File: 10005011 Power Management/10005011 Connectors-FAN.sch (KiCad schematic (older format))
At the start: 63 parts, among them IC25 L78M24CDT, IC6 TLV3012AIDBV, J10 BATTERY, J6 FAN, J7 CPU BOARD, J9 TURBINE, T23 IRLML2803, T31 IRLML5103

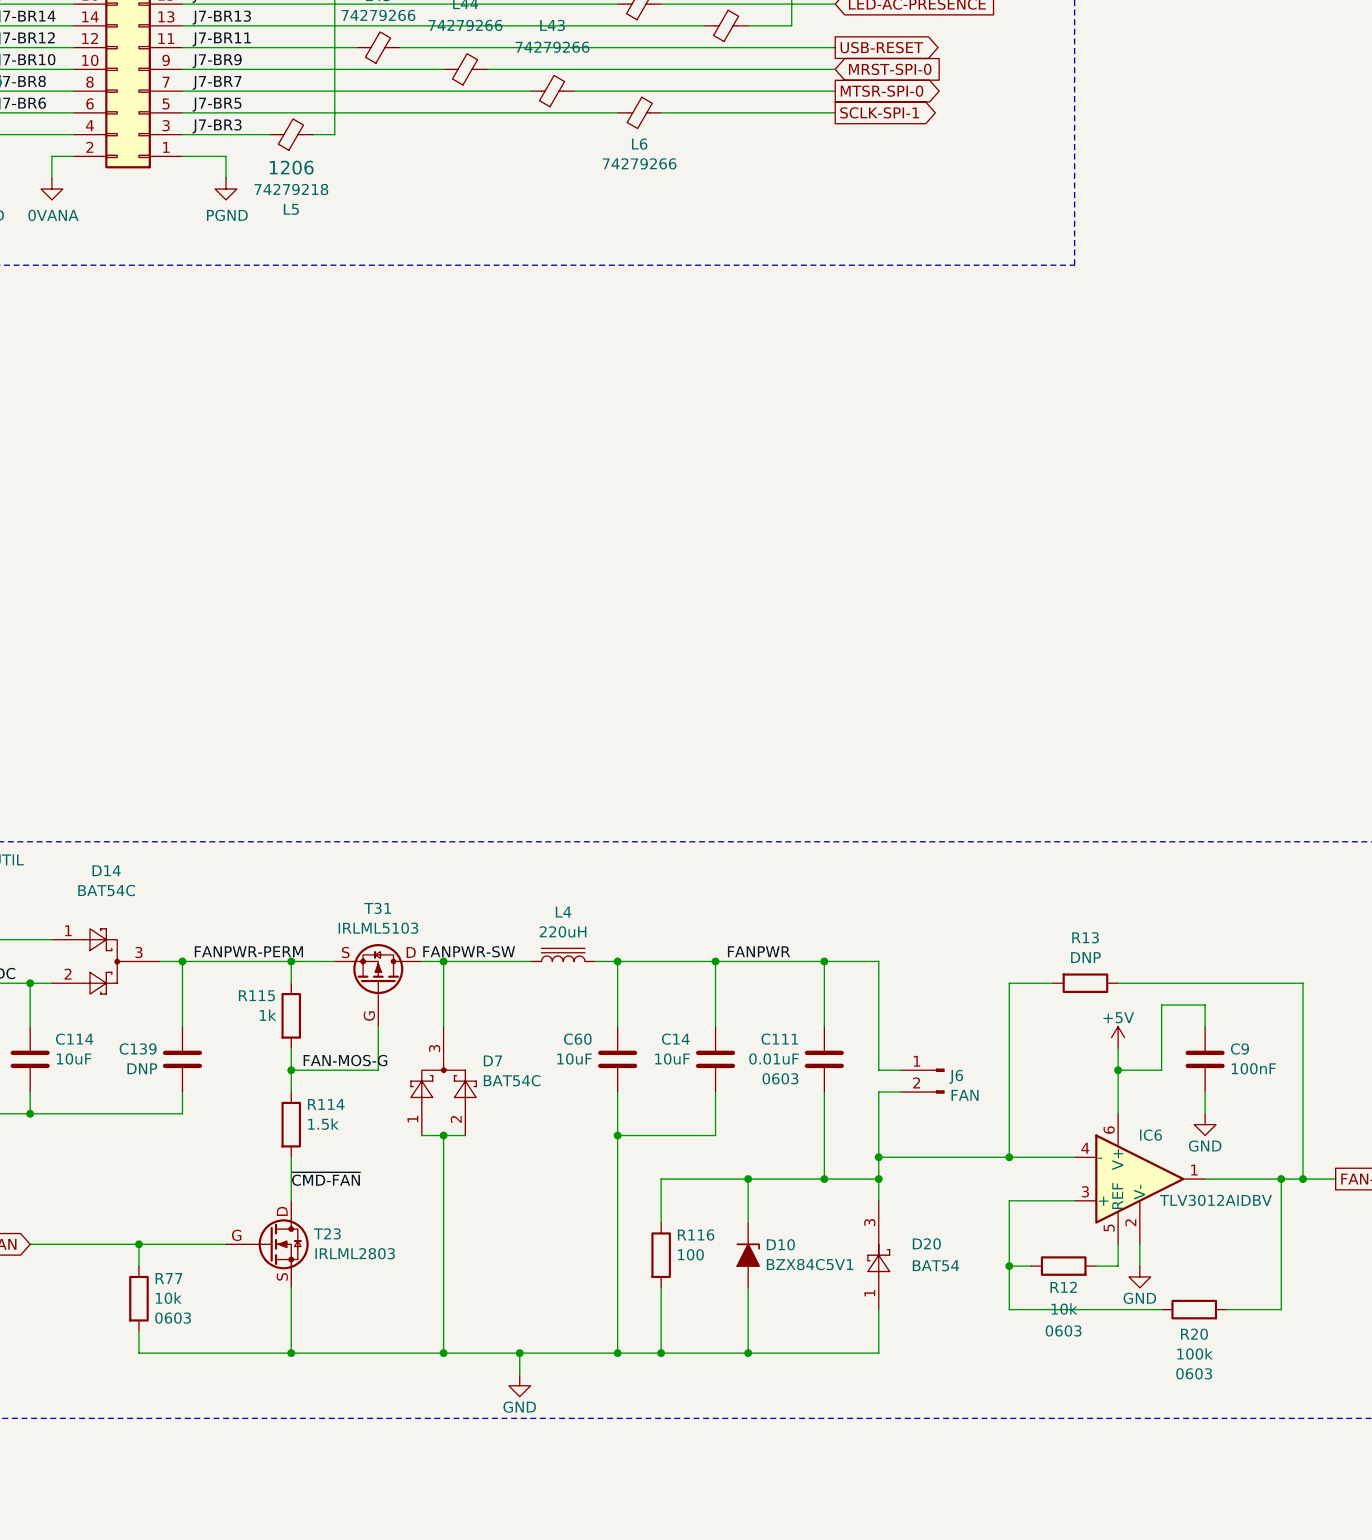
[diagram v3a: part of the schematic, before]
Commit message: Power managmt: fields updated from library, and non-library fields removed
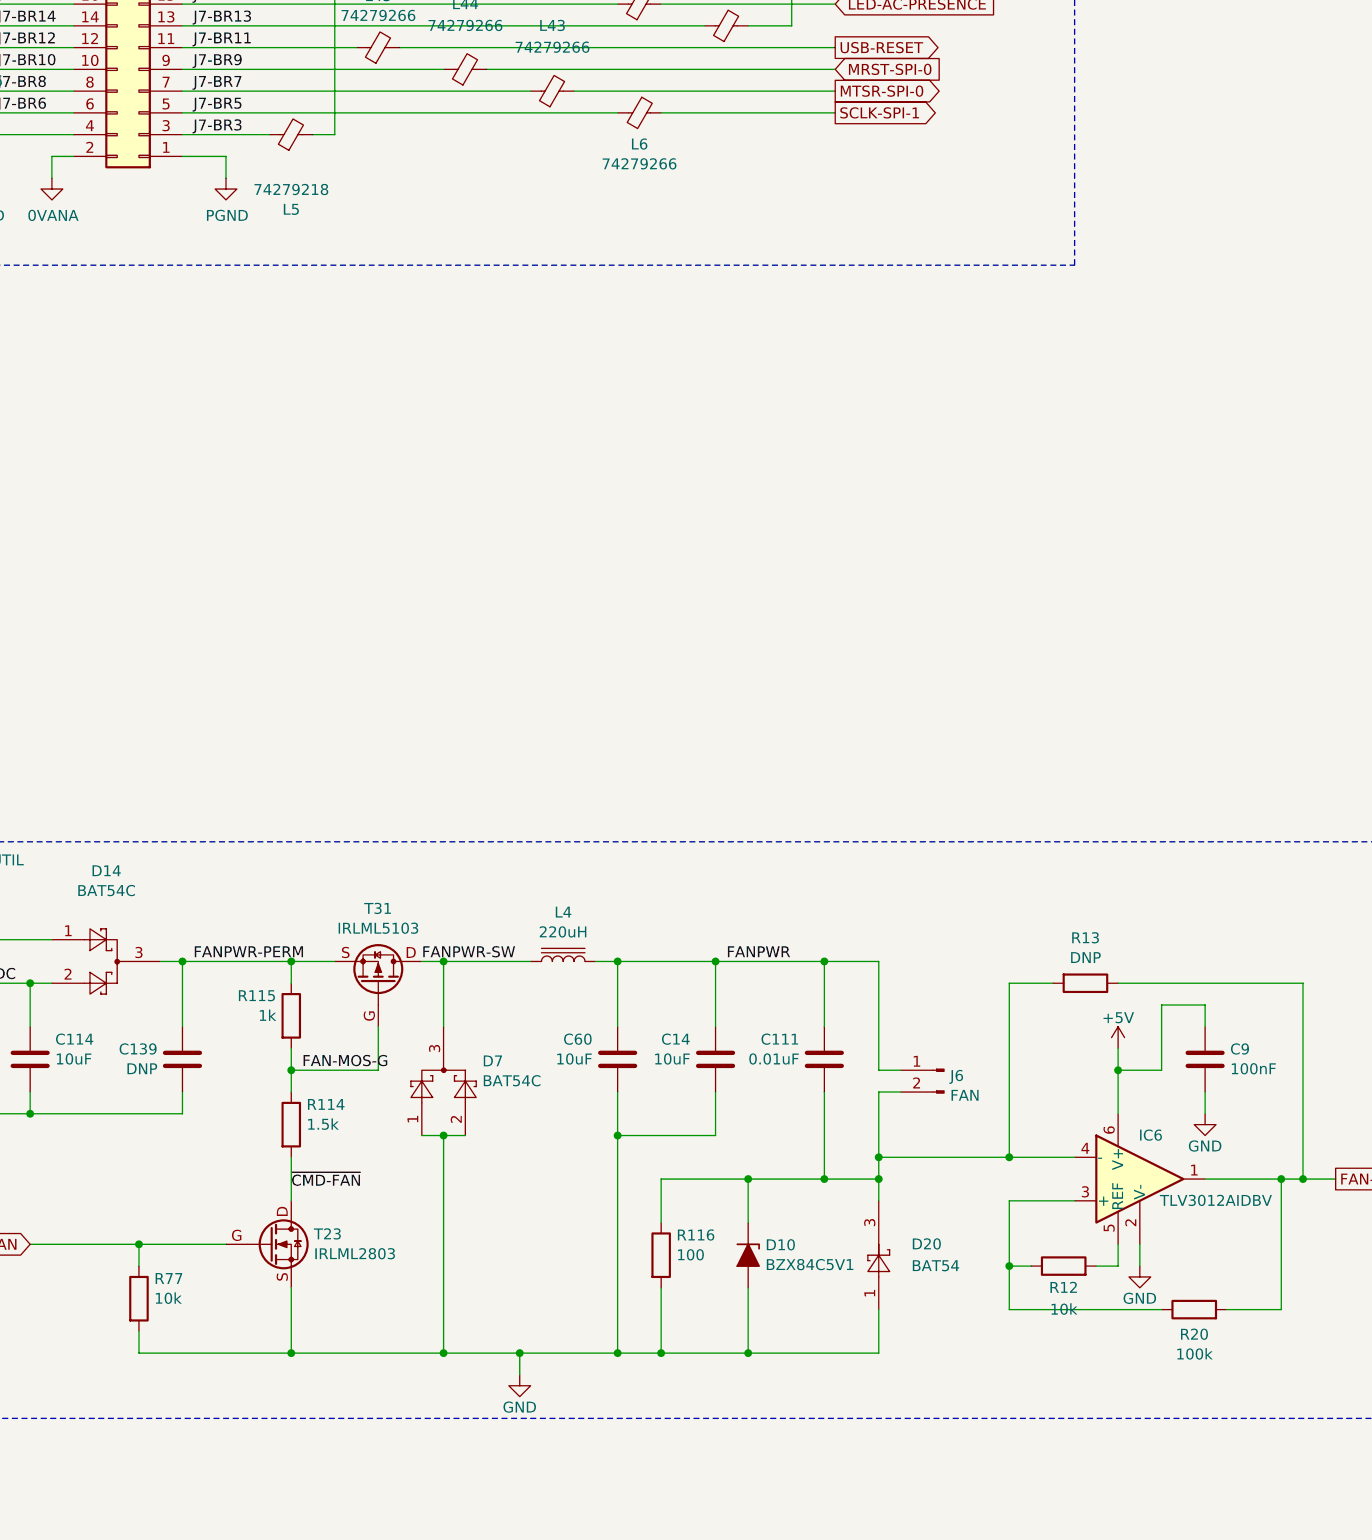
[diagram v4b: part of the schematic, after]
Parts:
- C10, C114, C14, C60: Description CAPACITOR CERAMIC, 10UF,+/-10%,50V -> CAPACITOR CERAMIC, 10UF,+/-10%,50V 2220; Dielectric X7R -> (none); Manufacturer2 (none) -> KEMET_RMS1; Manufacturer3 (none) -> KEMET_RMS1; Manufacturer_No2 (none) -> C2220X106K5RACAUTO; Manufacturer_No3 (none) -> C2220X106K5RAC; Mfgr TDK Corporation -> (none); Mfgr_PN CGA9N3X7R1H106K230KB -> (none); Source Digi-Key -> (none); Source_PN 445-7932-1-ND -> (none); Voltage 50V -> (none)
- C100, C61, C62, C98: Manufacturer (none) -> YAGEO_RMS1; Manufacturer2 (none) -> AVX_RMS1; Manufacturer_No (none) -> CA0612KRNPO9BN470; Manufacturer_No2 (none) -> W3A45A470KAT2A; Mfgr KEMET -> (none); Mfgr_PN CA064C470K5GAC7800 -> (none); Source Digi-Key -> (none); Source_PN 399-10028-1-ND -> (none)
- C109, C110, C112, C113: Dielectric X7R -> (none); Manufacturer (none) -> YAGEO_RMS1; Manufacturer2 (none) -> MURATA MANUFACTURING CO., LTD.; Manufacturer3 (none) -> YAGEO_RMS1; Manufacturer_No (none) -> CC0805KRX7R9BB104; Manufacturer_No2 (none) -> GRM21BR71H104KA01L; Manufacturer_No3 (none) -> CC0805KRX7R9BB104; Mfgr Yageo -> (none); Mfgr_PN CC0805KRX7R9BB104 -> (none); Source Digi-Key -> (none); Source_PN 311-1140-1-ND -> (none); Voltage 50V -> (none)
- C111: Bom_Footprint 0603 -> (none); Description CAP CER 10000PF 50V X7R 0603 -> CAPACITOR CERAMIC,10NF,+/-10%,50V,0603; Dielectric X7R -> (none); Item Number (none) -> 10022508; Manufacturer (none) -> YAGEO_RMS1; Manufacturer2 (none) -> YAGEO_RMS1; Manufacturer3 (none) -> KEMET_RMS1; Manufacturer_No (none) -> CC0603KRX7R9BB103; Manufacturer_No2 (none) -> CC0603KRX7R9BB104; Manufacturer_No3 (none) -> C0603C103K5RACTU; Mfgr Yageo -> (none); Mfgr_PN CC0603KRX7R9BB103 -> (none); Source Digi-Key -> (none); Source_PN 311-1085-1-ND -> (none); Voltage 50V -> (none)
- C53: Dielectric NPO -> (none); Manufacturer (none) -> YAGEO_RMS1; Manufacturer2 (none) -> AVX_RMS1; Manufacturer_No (none) -> CA0612KRNPO9BN470; Manufacturer_No2 (none) -> W3A45A470KAT2A; Mfgr KEMET -> (none); Mfgr_PN CA064C470K5GAC7800 -> (none); Notes Need to create a footprint -> (none); Source Digi-Key -> (none); Source_PN 399-10028-1-ND -> (none); Voltage 50V -> (none)
- C9: Dielectric X7R -> (none); Manufacturer2 (none) -> YAGEO_RMS1; Manufacturer3 (none) -> YAGEO_RMS1; Manufacturer_No2 (none) -> CC0402KRX7R7BB104; Manufacturer_No3 (none) -> CC0402KRX7R7BB104; Mfgr Yageo -> (none); Mfgr_PN CC0603KRX7R9BB103 -> (none); Source Digi-Key -> (none); Source_PN 311-1085-1-ND -> (none); Voltage 50V -> (none)
- D10: Manufacturer (none) -> NXP SEMICONDUCTORS_RMS1; Manufacturer2 (none) -> NXP SEMICONDUCTORS_RMS1; Manufacturer_No (none) -> BZX84-C5V1; Manufacturer_No2 (none) -> BZX84-C5V1,215; Mfgr Diodes Incorporated -> (none); Mfgr_PN BZX84C5V1-7-F -> (none); Source Digi-Key -> (none); Source_PN BZX84C5V1-FDITR-ND -> (none)
- D14, D7: Description DIODE ARRAY SCHOTTKY 30V SOT23-3 -> DIODE SCHOTTKY DOUBLE,30V, 200MA,SOT23; Manufacturer (none) -> NXP SEMICONDUCTORS_RMS1; Manufacturer2 (none) -> NXP SEMICONDUCTORS_RMS1; Manufacturer_No (none) -> BAT54C,215; Manufacturer_No2 (none) -> BAT54C; Mfgr ON Semiconductor -> (none); Mfgr_PN BAT54C -> (none); Source Digi-Key -> (none); Source_PN BAT54CFSCT-ND -> (none)
- D20: Description DIODE SCHOTTKY 30V 200MA SOT23-3 -> DIODE SCHOTTKY, 30V, 200MA; Manufacturer (none) -> NXP SEMICONDUCTORS_RMS1; Manufacturer2 (none) -> NXP SEMICONDUCTORS_RMS1; Manufacturer_No (none) -> BAT54,215; Manufacturer_No2 (none) -> BAT54; Mfgr ON Semiconductor -> (none); Mfgr_PN BAT54LT1G -> (none); Source Digi-Key -> (none); Source_PN BAT54LT1GOSTR-ND -> (none)
- D21: Description TVS DIODE 36V 58.1V SMB -> DIODE TRANSIENT 600W,36V; Manufacturer (none) -> LITTLEFUSE; Manufacturer2 (none) -> LITTLEFUSE; Manufacturer3 (none) -> ON SEMICONDUCTOR_RMS1; Manufacturer_No (none) -> SZ1SMB36AT3G; Manufacturer_No2 (none) -> 1SMB36AT3G; Manufacturer_No3 (none) -> 1SMB36AT3G; Mfgr Littelfuse Inc. -> (none); Mfgr_PN SZ1SMB36AT3G -> (none); Source Digi-Key -> (none); Source_PN F11561CT-ND -> (none)
- IC25: Description (none) -> IC,REGULATOR, 24V +/-4%, 500MA, DPACK; Item Number (none) -> 10022904; Manufacturer (none) -> ST MICROELECTRONIC; Manufacturer2 (none) -> ST MICROELECTRONIC; Manufacturer_No (none) -> L78M24CDT-TR; Manufacturer_No2 (none) -> L78M24CDT
- IC6: Manufacturer TEXAS INSTRUMENTS -> TEXAS INSTRUMENTS_RMS1; Manufacturer2 (none) -> TEXAS INSTRUMENTS_RMS1; Manufacturer_No2 (none) -> TLV3012AIDBVTG4
- J10: Description (none) -> CONNECTOR FEMALE,2.54MM SPACING,8.5MM +/-0.15; Item Number (none) -> 10022875; Manufacturer (none) -> HARWIN (012775); Manufacturer2 (none) -> MOLEX_RMS1; Manufacturer_No (none) -> M20-7830546; Manufacturer_No2 (none) -> 90151-2210
- J6: Description (none) -> CONNECTOR HEADER, 2 CIRCUITS, 2.54MM, 4A, 250V; Item Number (none) -> 10022872; Manufacturer (none) -> MOLEX_RMS1; Manufacturer_No (none) -> 22-27-2021
- J7: Description (none) -> HEADER CONNECTOR, VERTICAL, 26 PINS; Item Number (none) -> 10052332; Manufacturer (none) -> FCI/BERG; Manufacturer2 (none) -> FCI/BERG; Manufacturer_No (none) -> 75869-105LF; Manufacturer_No2 (none) -> 88880-013LF
- J9: Manufacturer MOLEX -> MOLEX_RMS1
- JPL2, JPL3: Description (none) -> RESISTANCE, 0 OHM,0603; Item Number (none) -> 10023185; Manufacturer (none) -> YAGEO_RMS1; Manufacturer2 (none) -> YAGEO_RMS1; Manufacturer3 (none) -> YAGEO_RMS1; Manufacturer_No (none) -> RC0603JR-070RL; Manufacturer_No2 (none) -> RC0603JR-070RL; Manufacturer_No3 (none) -> RC0603JR-070RL
- L15, L16, L17, L18, L19, L20, L21, L22, L23, L43, L44, L45, L46, L47, L48, L49, L50, L6: Description FERRITE BEAD 1 KOHM 0603 1LN -> SMD FERRITE 200MA; Manufacturer (none) -> WURTH ELEKTRONIK GMBH; Manufacturer_No (none) -> 74279266; Mfgr Würth Elektronik -> (none); Mfgr_PN 74279266 -> (none); Source Digi-Key -> (none); Source_PN 732-4484-1-ND -> (none)
- L4: Description (none) -> INDUCTOR, MINIATURE, 220UH, 220MA,WE-TPC; Item Number (none) -> 10022910; Manufacturer (none) -> WURTH ELEKTRONIK GMBH; Manufacturer_No (none) -> 74455222
- L5: Bom_Footprint 1206 -> (none); Manufacturer (none) -> WURTH ELEKTRONIK GMBH; Manufacturer_No (none) -> 74279218; Mfgr Würth Elektronik -> (none); Mfgr_PN 74279218 -> (none); Source Digi-Key -> (none); Source_PN 732-1623-1-ND -> (none)
- L61: Description FERRITE BEAD 600 OHM 1206 1LN -> SMD FERRITE, 1A,1206; Manufacturer (none) -> WURTH ELEKTRONIK GMBH; Manufacturer_No (none) -> 74279218; Mfgr Würth Elektronik -> (none); Mfgr_PN 74279218 -> (none); Source Digi-Key -> (none); Source_PN 732-1623-1-ND -> (none)
- ML2, ML3: Manufacturer (none) -> EPCOS_RMS1; Manufacturer_No (none) -> B72500T0040M060; Mfgr TDK Electronics Inc. -> (none); Mfgr_PN B72500T0040M060 -> (none); Source Digi-Key -> (none); Source_PN 495-2595-1-ND -> (none)
- PT1: Description (none) -> TEST POINT; Item Number (none) -> 10022924; Manufacturer (none) -> NICOMATIC_RMS1; Manufacturer2 (none) -> KEYSTONE ELECTRONICS CORP; Manufacturer_No (none) -> C12000B; Manufacturer_No2 (none) -> 5015
- R114: Manufacturer (none) -> YAGEO_RMS1; Manufacturer2 (none) -> BOURNS_RMS1; Manufacturer3 (none) -> YAGEO_RMS1; Manufacturer_No (none) -> RC1206FR-071K5L; Manufacturer_No2 (none) -> CR1206-FX-1501ELF; Manufacturer_No3 (none) -> RC1206FR-071K5L; Mfgr YAGEO_RMS1 -> (none); Mfgr_PN RC1206FR-071K5L -> (none)
- R115: Manufacturer (none) -> SAMSUNG_RMS1; Manufacturer2 (none) -> YAGEO_RMS1; Manufacturer3 (none) -> YAGEO_RMS1; Manufacturer_No (none) -> RC3216F1001CS; Manufacturer_No2 (none) -> RC1206FR-071KL; Manufacturer_No3 (none) -> RC1206FR-071KL; Mfgr YAGEO_RMS1 -> (none); Mfgr_PN RC1206FR-071KL -> (none)
- R116: Manufacturer No 232272461001L -> (none); Manufacturer2 (none) -> BOURNS_RMS1; Manufacturer3 (none) -> YAGEO/PHYCOMP_RMS1; Manufacturer_No (none) -> RC1206FR-07100RL; Manufacturer_No2 (none) -> CR1206-FX-1000ELF; Manufacturer_No3 (none) -> RC1206FR-07100RL
- R12, R77: Bom_Footprint 0603 -> (none); Description RES SMD 10K OHM 1% 1/10W 0603 -> RESISTOR,10K OHM.0.063W,+/-1%,0603; Item Number (none) -> 10022548; Manufacturer (none) -> YAGEO_RMS1; Manufacturer2 (none) -> SAMSUNG_RMS1; Manufacturer3 (none) -> BOURNS_RMS1; Manufacturer_No (none) -> RC0603FR-0710KL; Manufacturer_No2 (none) -> RC1608F103CS; Manufacturer_No3 (none) -> CR0603-FX-1002ELF; Mfgr Yageo -> (none); Mfgr_PN RC0603FR-0710KL -> (none); Source Digi-Key -> (none); Source_PN 311-10.0KHRCT-ND -> (none); Tolerance 1% -> (none); Wattage 1/10W -> (none)
- R20: Bom_Footprint 0603 -> (none); Description RES SMD 100K OHM 1% 1/10W 0603 -> RESISTOR,100KOHM,0.063W,+/-1%,0603; Item Number (none) -> 10022549; Manufacturer (none) -> YAGEO_RMS1; Manufacturer2 (none) -> BOURNS_RMS1; Manufacturer3 (none) -> YAGEO_RMS1; Manufacturer_No (none) -> RC0603FR-07100KL; Manufacturer_No2 (none) -> CR0603-FX-1003ELF; Manufacturer_No3 (none) -> RC0603FR-07100KL; Mfgr Yageo -> (none); Mfgr_PN RC0603FR-07100KL -> (none); Source Digi-Key -> (none); Source_PN 311-100KHRTR-ND -> (none); Tolerance 1% -> (none); Wattage 1/10W -> (none)
- R78: Manufacturer (none) -> SUSUMU CO; Manufacturer2 (none) -> YAGEO_RMS1; Manufacturer3 (none) -> SUSUMU CO; Manufacturer_No (none) -> RG1608P-103-B-T1; Manufacturer_No2 (none) -> RT0603BRB0710KL; Manufacturer_No3 (none) -> RG1608P-103-B-T5; Mfgr Panasonic Electronic Components -> (none); Mfgr_PN ERA-3AEB103V -> (none); Source Digi-Key -> (none); Source_PN P10KDBCT-ND -> (none)
- T23: Manufacturer (none) -> INTERNATIONAL RECTIFIER_RMS1; Manufacturer2 (none) -> INTERNATIONAL RECTIFIER_RMS1; Manufacturer_No (none) -> IRLML2803PBF; Manufacturer_No2 (none) -> IRLML2803TRPBF; Mfgr Infineon Technologies -> (none); Mfgr_PN IRLML2803TRPBF -> (none); Source Digi-Key -> (none); Source_PN IRLML2803PBFCT-ND -> (none)
- T31: Description MOSFET P-CH 30V 760MA SOT-23 -> RSPTRANSISTOR MOSFET, P CHANNEL, 30V,0.6A; Manufacturer (none) -> INTERNATIONAL RECTIFIER_RMS1; Manufacturer_No (none) -> IRLML5103TRPBF; Mfgr Infineon Technologies -> (none); Mfgr_PN IRLML5103TRPBF -> (none); Source Digi-Key -> (none); Source_PN IRLML5103PBFCT-ND -> (none)

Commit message: added test point with two pins in symbol library for nicomatic C12000B part
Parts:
- PT1: symbol V_Connector:TestPoint -> V_Connector:TestPoint_2
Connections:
- net 0VANA: now also PT1.2
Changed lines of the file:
@@
 	3200 7300 3200 7400
 $Comp
-L V_Power:PGND #PWR?
+L V_Power:PGND #PWR0167
 U 1 1 5EE6252B
 P 5500 7350
-F 0 "#PWR?" H 5500 7100 50  0001 C CNN
+F 0 "#PWR0167" H 5500 7100 50  0001 C CNN
 F 1 "PGND" H 5500 7200 50  0000 C CNN
 F 2 "" H 5500 7350 50  0001 C CNN
@@
 $EndComp
 $Comp
-L V_Connector:TestPoint PT1
+L V_Connector:TestPoint_2 PT1
 U 1 1 5EB70271
 P 4300 7875

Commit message: Updated schematics from library
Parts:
- C9: Manufacturer MURATA -> YAGEO_RMS1; Manufacturer3 YAGEO_RMS1 -> MURATA MANUFACTURING CO., LTD.; Manufacturer_No GRM155R71C104JA88J -> CC0402KRX7R7BB104; Manufacturer_No2 CC0402KRX7R7BB104 -> 223878715649; Manufacturer_No3 CC0402KRX7R7BB104 -> GRM155R71C104KA88D
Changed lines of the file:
@@
 F 1 "IRLML2803" H 9754 8305 50  0000 L CNN
 F 2 "AllModules:SOT23-GSD_1" H 10500 8275 50  0001 C CIN
-F 3 "" H 9875 8050 50  0001 L CNN
+F 3 "https://www.infineon.com/dgdl/irlml2803pbf.pdf?fileId=5546d462533600a4015356682aff260f" H 9875 8050 50  0001 L CNN
 F 4 "TRANSISTOR MOSFET, 30V, 0.93A, 0.25 OHM, N CHANNEL" H 10350 8275 50  0001 C CNN "Description"
 F 5 "10022558" H 9550 8350 50  0001 C CNN "Item Number"
@@
 F 4 "CAPACITOR,100NF,16V,+/-10%,X7R,0402" H 13850 7500 50  0001 C CNN "Description"
 F 5 "10022607" H 13850 7500 50  0001 C CNN "Item Number"
-F 6 "MURATA" H 13850 7500 50  0001 C CNN "Manufacturer"
-F 7 "GRM155R71C104JA88J" H 13850 7500 50  0001 C CNN "Manufacturer_No"
+F 6 "YAGEO_RMS1" H 13850 7500 50  0001 C CNN "Manufacturer"
+F 7 "CC0402KRX7R7BB104" H 13850 7500 50  0001 C CNN "Manufacturer_No"
 F 8 "YAGEO_RMS1" H 0   0   50  0001 C CNN "Manufacturer2"
-F 9 "YAGEO_RMS1" H 0   0   50  0001 C CNN "Manufacturer3"
-F 10 "CC0402KRX7R7BB104" H 0   0   50  0001 C CNN "Manufacturer_No2"
-F 11 "CC0402KRX7R7BB104" H 0   0   50  0001 C CNN "Manufacturer_No3"
+F 9 "MURATA MANUFACTURING CO., LTD." H 0   0   50  0001 C CNN "Manufacturer3"
+F 10 "223878715649" H 0   0   50  0001 C CNN "Manufacturer_No2"
+F 11 "GRM155R71C104KA88D" H 0   0   50  0001 C CNN "Manufacturer_No3"
 	1    13850 7500
 	1    0    0    -1
